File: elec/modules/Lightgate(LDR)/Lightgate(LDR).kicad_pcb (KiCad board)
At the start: 2 copper layers, 24.4 x 47.7 mm, 2 parts, among them J1 Conn_01x02

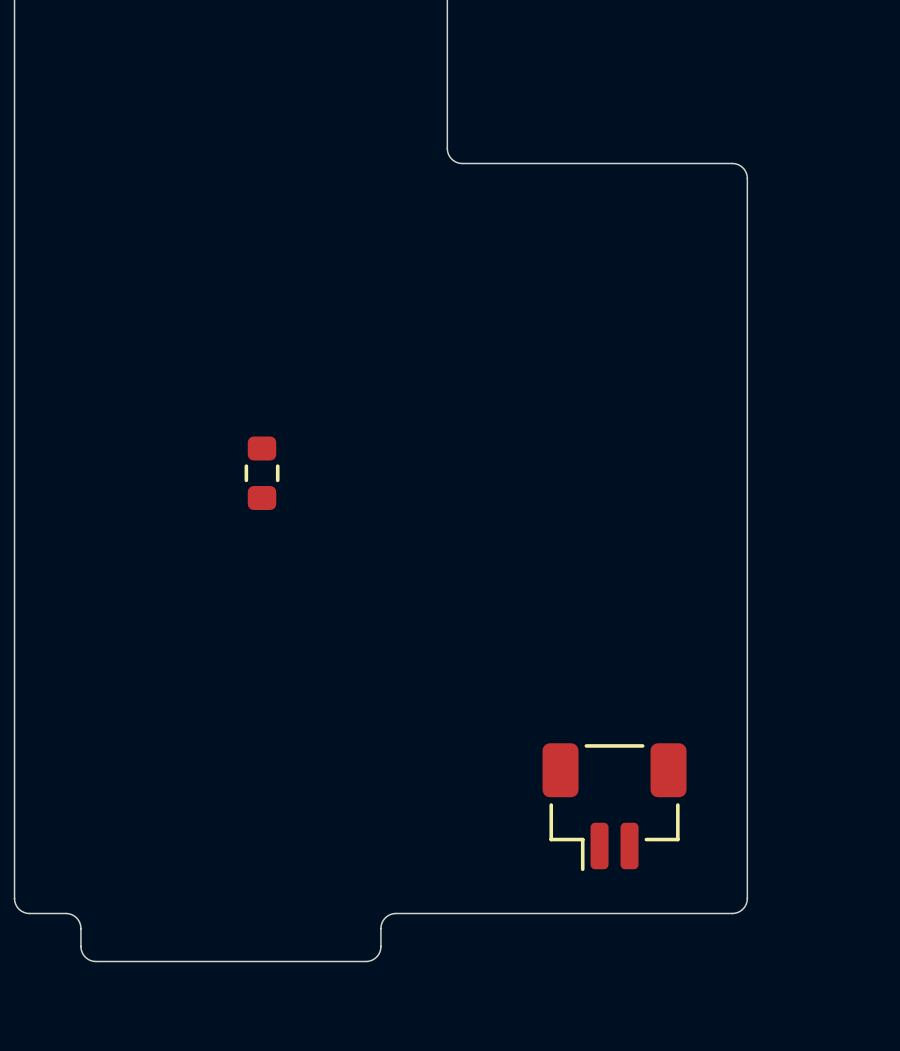
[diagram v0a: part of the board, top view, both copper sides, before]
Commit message: fixed light gate jst
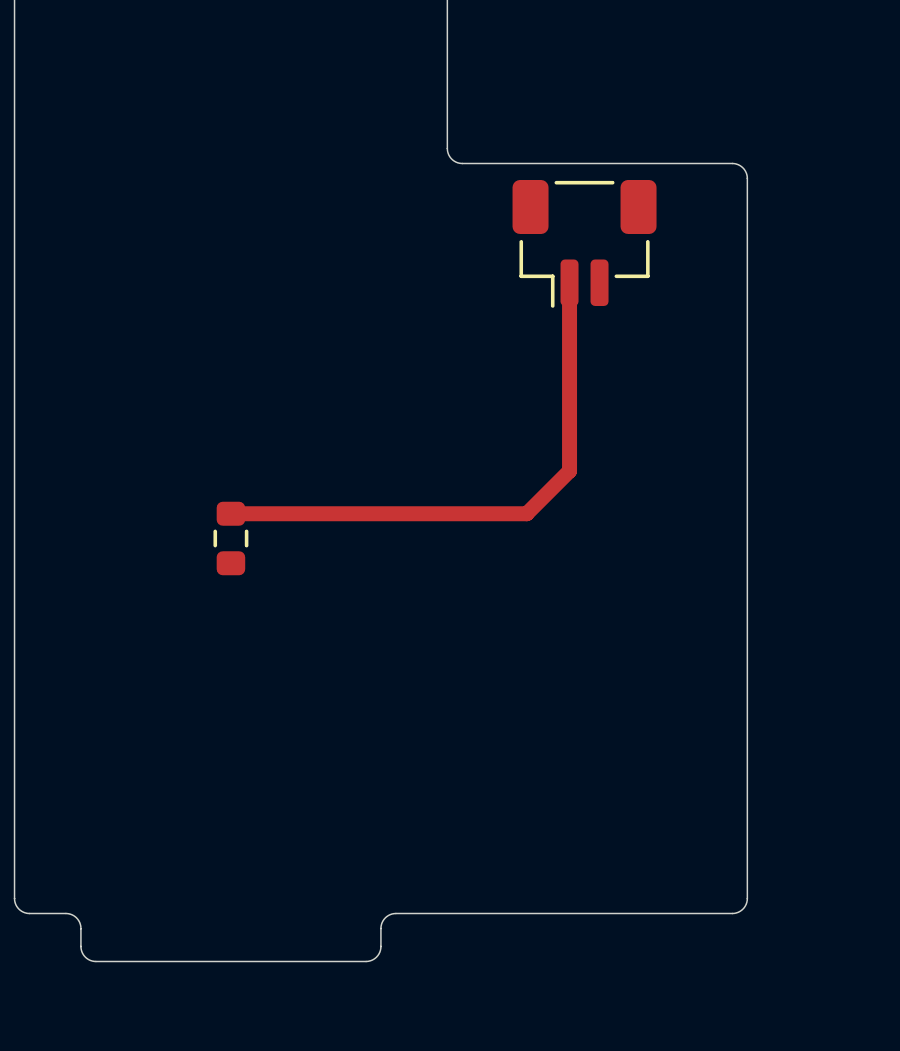
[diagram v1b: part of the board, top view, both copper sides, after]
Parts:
- moved J1 18.8 mm to (161.8, 95.9)
- moved LED_2 2.41 mm to (150.0, 105.8)
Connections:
- J1 pad 1: +3V3 -> /LightGateLDR
- J1 pad 2: /LightGateLDR -> +3V3
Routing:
- net /LightGateLDR: track 0.00 -> 18.2 mm
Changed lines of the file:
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@@
 	(footprint "Resistor_SMD:R_0603_1608Metric"
 		(layer "F.Cu")
-		(at 151 103.575 90)
+		(at 149.963441 105.750006 90)
 		(descr "Resistor SMD 0603 (1608 Metric), square (rectangular) end terminal, IPC-7351 nominal, (Body size source: IPC-SM-782 page 72, https://www.pcb-3d.com/wordpress/wp-content/uploads/ipc-sm-782a_amendment_1_and_2.pdf), generated with kicad-footprint-generator")
 		(tags "resistor")
@@
 		(property ki_fp_filters "*LDR* R?LDR*")
 		(sheetname "/")
-		(sheetfile "Lightfgate(LDR).kicad_sch")
+		(sheetfile "Lightgate(LDR).kicad_sch")
 		(attr smd)
 		(fp_line
@@
 	(footprint "Connector_JST:JST_SH_BM02B-SRSS-TB_1x02-1MP_P1.00mm_Vertical"
 		(layer "F.Cu")
-		(at 162.75 114.675)
+		(at 161.75 95.9)
 		(descr "JST SH series connector, BM02B-SRSS-TB (http://www.jst-mfg.com/product/pdf/eng/eSH.pdf), generated with kicad-footprint-generator")
 		(tags "connector JST SH vertical")
@@
 		(property ki_fp_filters "Connector*:*_1x??_*")
 		(sheetname "/")
-		(sheetfile "Lightfgate(LDR).kicad_sch")
+		(sheetfile "Lightgate(LDR).kicad_sch")
 		(attr smd)
 		(fp_line
@@
 			(layers "F.Cu" "F.Mask" "F.Paste")
 			(roundrect_rratio 0.25)
-			(net 2 "+3V3")
+			(net 1 "/LightGateLDR")
 			(pinfunction "Pin_1")
 			(pintype "passive")
@@
 			(layers "F.Cu" "F.Mask" "F.Paste")
 			(roundrect_rratio 0.25)
-			(net 1 "/LightGateLDR")
+			(net 2 "+3V3")
 			(pinfunction "Pin_2")
 			(pintype "passive")
@@
 		)
 		(embedded_fonts no)
-		(model "${KICAD9_3DMODEL_DIR}/Connector_JST.3dshapes/JST_SH_BM02B-SRSS-TB_1x02-1MP_P1.00mm_Vertical.step"
+		(model "C:/Users/Eusto/Documents/Cup/robocup2026-i2/elec/modules/references/LightGatejst 3d model/S2B-PH-SM4-TB--3DModel-STEP-269445.STEP"
 			(offset
-				(xyz 0 0 0)
+				(xyz 0 5 0)
 			)
 			(scale
@@
 			)
 			(rotate
-				(xyz 0 0 0)
+				(xyz -90 -0 -180)
 			)
 		)
@@
 		(layer "Edge.Cuts")
 	)
-	(dimension
-		(type orthogonal)
+	(segment
+		(start 161.25 103.5)
+		(end 161.25 97.225)
+		(width 0.5)
 		(layer "F.Cu")
-		(pts
-			(xy 162.75 114.675) (xy 162.75 118.25)
-		)
-		(height -5)
-		(orientation 1)
-		(format
-			(prefix "")
-			(suffix "")
-			(units 3)
-			(units_format 0)
-			(precision 4)
-			(suppress_zeroes yes)
-		)
-		(style
-			(thickness 0.2)
-			(arrow_length 1.27)
-			(text_position_mode 0)
-			(arrow_direction outward)
-			(extension_height 0.58642)
-			(extension_offset 0.5)
-			(keep_text_aligned yes)
-		)
-		(gr_text "3.575"
-			(at 155.95 116.4625 90)
-			(layer "F.Cu")
-			(effects
-				(font
-					(size 1.5 1.5)
-					(thickness 0.3)
-				)
-			)
-		)
-	)
-	(dimension
-		(type orthogonal)
+		(net 1)
+	)
+	(segment
+		(start 159.824994 104.925006)
+		(end 161.25 103.5)
+		(width 0.5)
 		(layer "F.Cu")
-		(pts
-			(xy 162.75 114.675) (xy 167.25 114.675)
-		)
-		(height 0)
-		(orientation 0)
-		(format
-			(prefix "")
-			(suffix "")
-			(units 3)
-			(units_format 0)
-			(precision 4)
-			(suppress_zeroes yes)
-		)
-		(style
-			(thickness 0.2)
-			(arrow_length 1.27)
-			(text_position_mode 0)
-			(arrow_direction outward)
-			(extension_height 0.58642)
-			(extension_offset 0.5)
-			(keep_text_aligned yes)
-		)
-		(gr_text "4.5"
-			(at 165 112.875 0)
-			(layer "F.Cu")
-			(effects
-				(font
-					(size 1.5 1.5)
-					(thickness 0.3)
-				)
-			)
-		)
+		(net 1)
+	)
+	(segment
+		(start 149.963441 104.925006)
+		(end 159.824994 104.925006)
+		(width 0.5)
+		(layer "F.Cu")
+		(net 1)
 	)
 	(zone
@@
 		(layers "F.Cu" "B.Cu")
 		(hatch edge 0.5)
-		(connect_pads
+		(connect_pads yes
 			(clearance 0.5)
 		)
@@
 			(thermal_gap 0.5)
 			(thermal_bridge_width 0.5)
+			(smoothing chamfer)
+			(radius 0.25)
 		)
 		(polygon
